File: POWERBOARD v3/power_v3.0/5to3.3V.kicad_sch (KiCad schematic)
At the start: 12 parts, among them IC2 MAX25301AATB_V+T, U3 TPS62160DSG

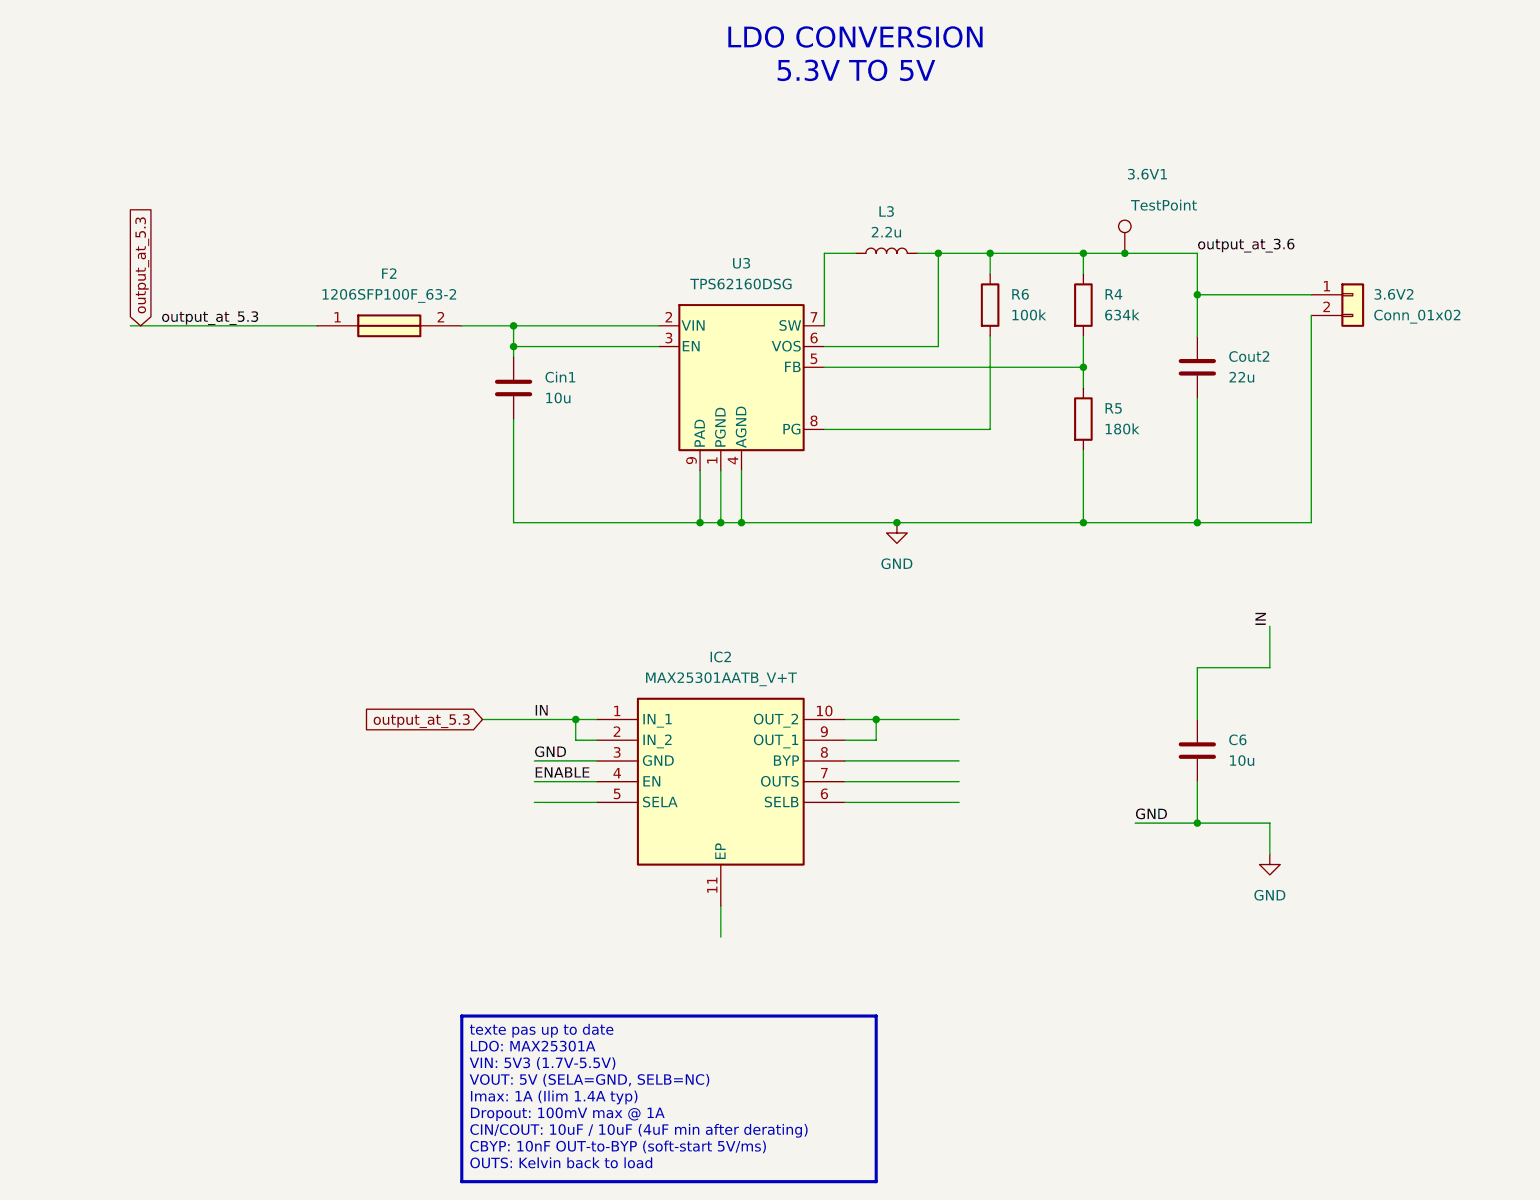
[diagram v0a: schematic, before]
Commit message: added TVS diodes to charging circuit and (almost fully) routed 5.3 to 5V LDO
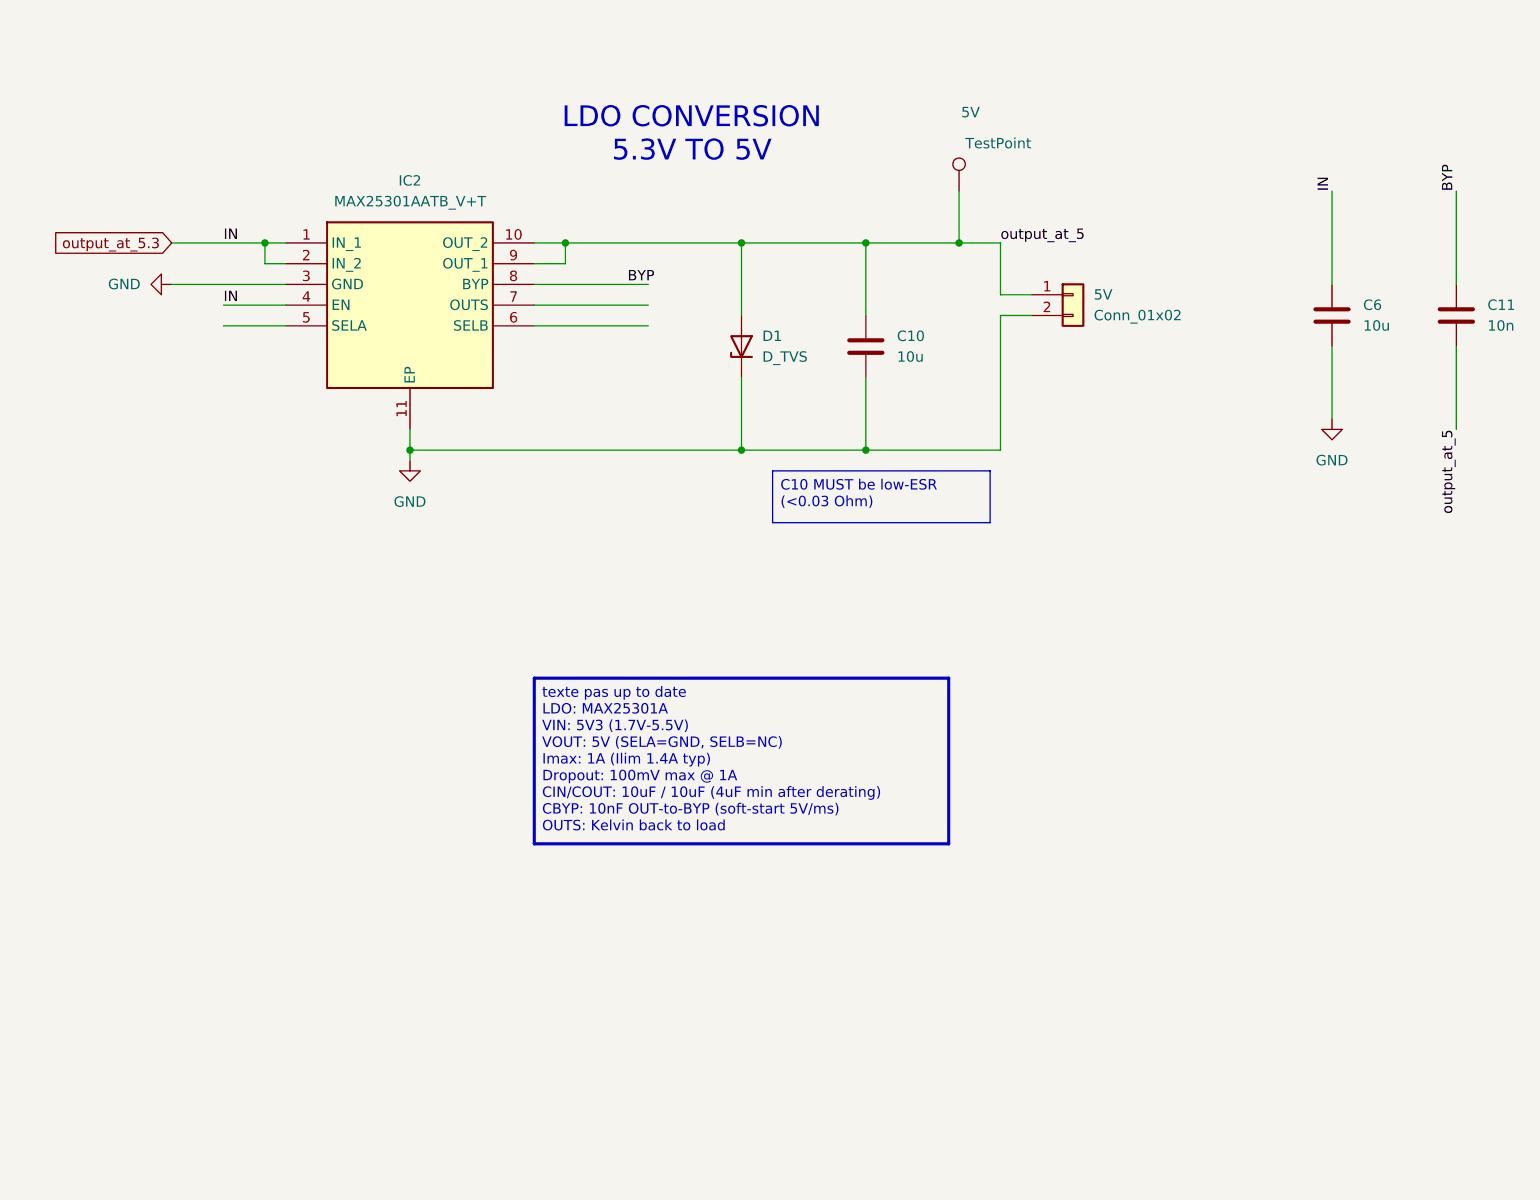
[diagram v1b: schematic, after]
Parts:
- removed 3.6V1: TestPoint, TestPoint:TestPoint_Keystone_5000-5004_Miniature, symbol Connector:TestPoint
- removed 3.6V2: Conn_01x02, Connector_PinHeader_2.00mm:PinHeader_1x02_P2.00mm_Vertical, symbol Connector_Generic:Conn_01x02
- removed Cin1: 10u, Capacitor_SMD:C_0805_2012Metric, symbol Device:C
- removed Cout2: 22u, Capacitor_SMD:C_1206_3216Metric, symbol Device:C
- removed F2: 1206SFP100F_63-2, Fuse:Fuse_1206_3216Metric, symbol 1206SFP100F_63-2:1206SFP100F_63-2
- removed L3: 2.2u, Inductor_SMD:L_Bourns-SRN4018, symbol Device:L
- removed R4: 634k, Resistor_SMD:R_0805_2012Metric, symbol Device:R
- removed R5: 180k, Resistor_SMD:R_0805_2012Metric, symbol Device:R
- removed R6: 100k, Resistor_SMD:R_0805_2012Metric, symbol Device:R
- removed U3: TPS62160DSG, Package_SON:WSON-8-1EP_2x2mm_P0.5mm_EP0.9x1.6mm_ThermalVias, symbol Regulator_Switching:TPS62160DSG
- added 5V: Conn_01x02, Connector_PinHeader_2.00mm:PinHeader_1x02_P2.00mm_Vertical, symbol Connector_Generic:Conn_01x02
- added 5V: TestPoint, TestPoint:TestPoint_Keystone_5000-5004_Miniature, symbol Connector:TestPoint
- added C10: 10u, symbol Device:C
- added C11: 10n, symbol Device:C
- added D1: D_TVS, Diode_THT:D_DO-41_SOD81_P10.16mm_Horizontal, symbol Device:D_Zener
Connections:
- net ENABLE is gone; now on net output_at_5.3: IC2.4 (EN)
- net GND: now also IC2.11 (EP), 5V.2 (Pin_2), C10.2, D1.1 (K)
- net output_at_5: now reaches IC2.10 (OUT_2), IC2.9 (OUT_1)
- net output_at_5: now also 5V.1, 5V.1 (Pin_1), C10.1, C11.2, D1.2 (A)
- net BYP: now reaches IC2.8 (BYP)
- net BYP: now also C11.1
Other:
- moved on the sheet: C6, IC2
